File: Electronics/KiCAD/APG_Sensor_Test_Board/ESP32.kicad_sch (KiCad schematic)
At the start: 4 parts, among them U1 ESP32-S3-WROOM-1

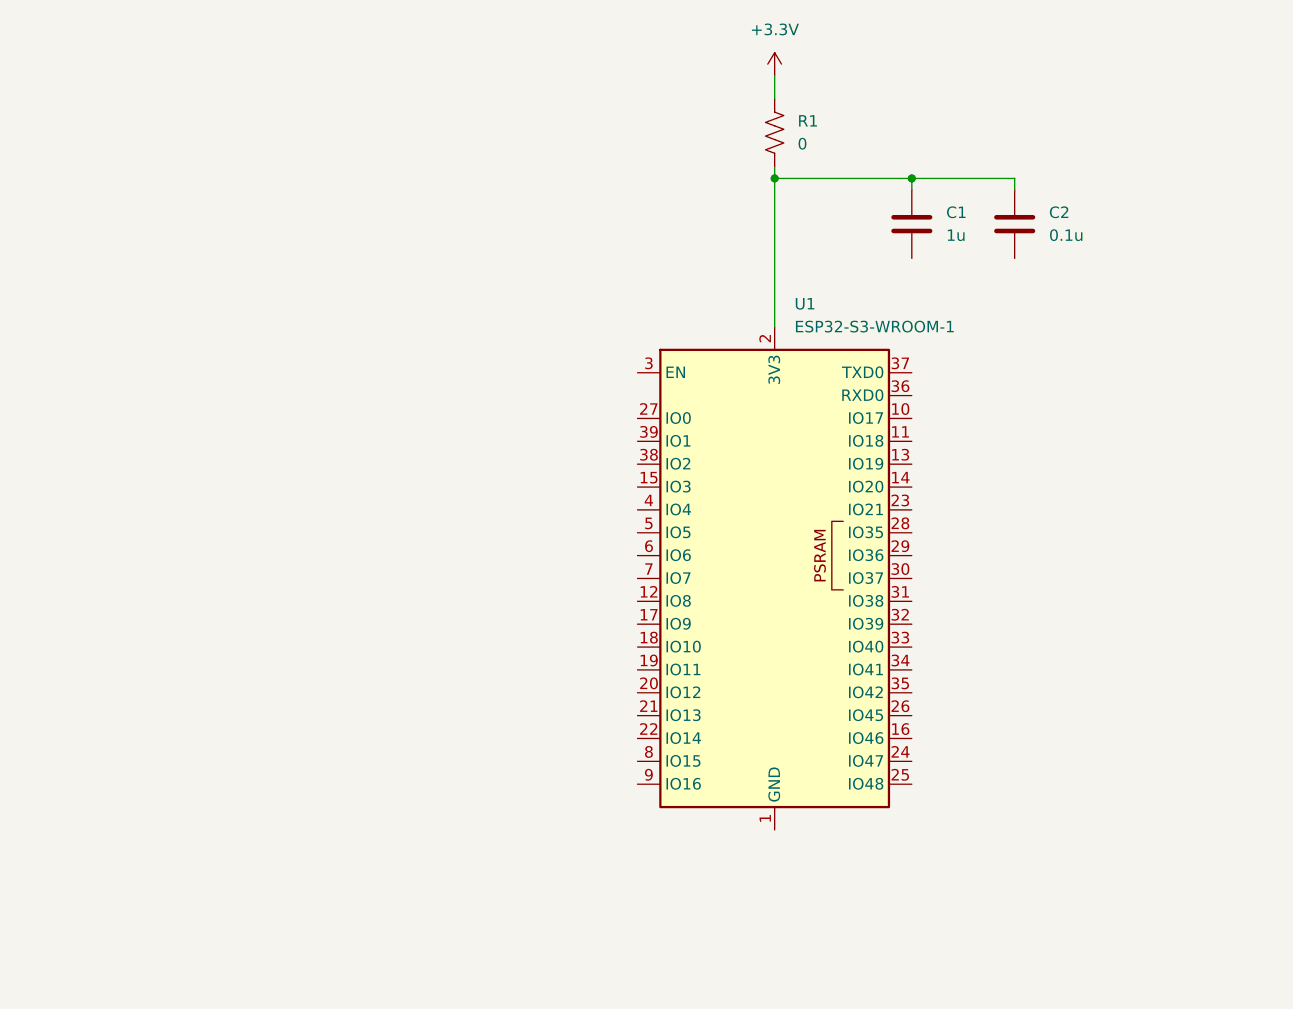
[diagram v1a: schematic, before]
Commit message: Gannon inspection decision to change IMU
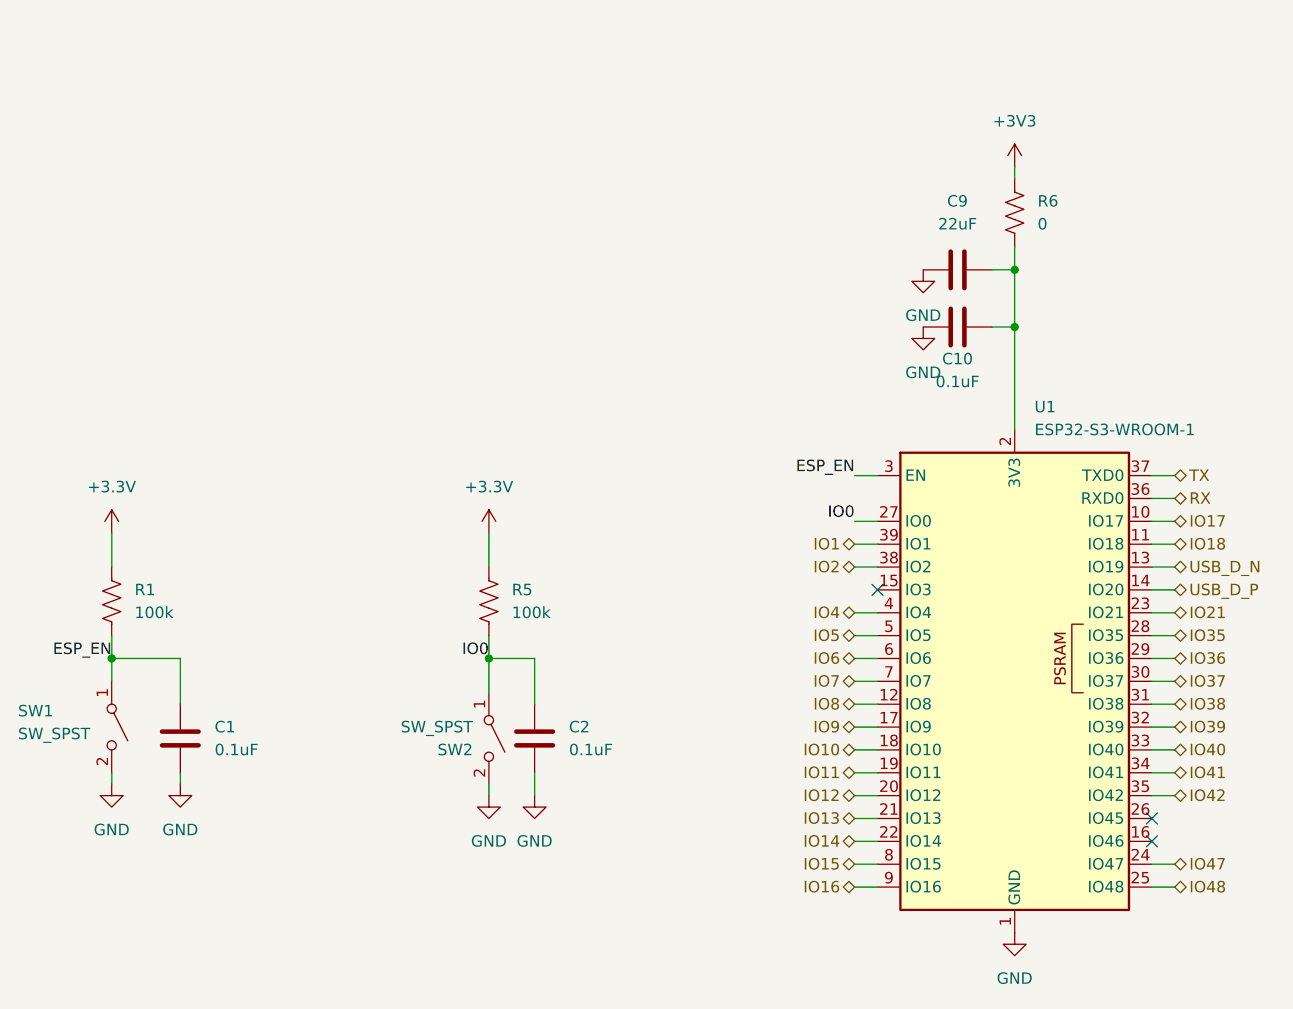
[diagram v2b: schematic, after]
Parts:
- added C10: 0.1uF, symbol Device:C
- added C9: 22uF, symbol Device:C
- added R5: 100k, symbol Device:R_US
- added R6: 0, symbol Device:R_US
- added SW1, SW2: SW_SPST, Button_Switch_SMD:SW_MEC_5GSH9, symbol Switch:SW_SPST
- C1: value 1u -> 0.1uF
- C2: value 0.1u -> 0.1uF
- R1: value 0 -> 100k
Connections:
- net +3.3V: now also R5.1
- net ESP_EN: now reaches C1.1, R1.2
- net ESP_EN: now also U1.3 (EN), SW1.1 (A); no longer C2.1, U1.2 (3V3)
- net GND: now reaches C1.2
- net GND: now also C2.2, U1.1 (GND), U1.40 (GND), U1.41 (GND), C10.1, C9.1, SW1.2 (B), SW2.2 (B)
- net IO17: now reaches U1.10 (IO17)
- net IO18: now reaches U1.11 (IO18)
- net IO8: now reaches U1.12 (IO8)
- net USB_D_N: now reaches U1.13 (IO19)
- net USB_D_P: now reaches U1.14 (IO20)
- net IO9: now reaches U1.17 (IO9)
- net IO10: now reaches U1.18 (IO10)
- net IO11: now reaches U1.19 (IO11)
- net IO12: now reaches U1.20 (IO12)
- net IO13: now reaches U1.21 (IO13)
- net IO14: now reaches U1.22 (IO14)
- net IO21: now reaches U1.23 (IO21)
- net IO47: now reaches U1.24 (IO47)
- net IO48: now reaches U1.25 (IO48)
- net IO0: now reaches U1.27 (IO0)
- net IO0: now also C2.1, R5.2, SW2.1 (A)
- net IO35: now reaches U1.28 (IO35)
- net IO36: now reaches U1.29 (IO36)
- net IO37: now reaches U1.30 (IO37)
- net IO38: now reaches U1.31 (IO38)
- net IO39: now reaches U1.32 (IO39)
- net IO40: now reaches U1.33 (IO40)
- net IO41: now reaches U1.34 (IO41)
- net IO42: now reaches U1.35 (IO42)
- net RX: now reaches U1.36 (RXD0)
- net TX: now reaches U1.37 (TXD0)
- net IO2: now reaches U1.38 (IO2)
- net IO1: now reaches U1.39 (IO1)
- net IO4: now reaches U1.4 (IO4)
- net IO5: now reaches U1.5 (IO5)
- net IO6: now reaches U1.6 (IO6)
- net IO7: now reaches U1.7 (IO7)
- net IO15: now reaches U1.8 (IO15)
- net IO16: now reaches U1.9 (IO16)
- new net: C10.2, C9.2, R6.2, U1.2 (3V3)
- new net +3V3: R6.1
- no-connect marks 0 -> 3

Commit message: reaninotate and begin footprints
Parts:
- C1, C2: footprint (none) -> Capacitor_SMD:C_0805_2012Metric
- C3: renamed from C9; footprint (none) -> Capacitor_SMD:C_0805_2012Metric
- C4: renamed from C10; footprint (none) -> Capacitor_SMD:C_0805_2012Metric
- R3: renamed from R1; footprint (none) -> Resistor_SMD:R_0805_2012Metric
- R4: renamed from R5; footprint (none) -> Resistor_SMD:R_0805_2012Metric
- R5: renamed from R6; footprint (none) -> Resistor_SMD:R_0805_2012Metric
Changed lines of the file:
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@@
 		(dnp no)
 		(fields_autoplaced yes)
-		(property "Reference" "#PWR01"
+		(property "Reference" "#PWR05"
 			(at 68.58 91.44 0)
 			(effects
@@
 			(project "APG_Sensor_Test_Board"
 				(path "/3161be0c-372f-463d-be0a-bab00f344057/597921f3-a65f-46ab-993f-3f9f1b9176d6"
-					(reference "#PWR01")
+					(reference "#PWR05")
 					(unit 1)
 				)
@@
 		(dnp no)
 		(fields_autoplaced yes)
-		(property "Reference" "#PWR025"
+		(property "Reference" "#PWR012"
 			(at 158.75 71.12 0)
 			(effects
@@
 			(project "APG_Sensor_Test_Board"
 				(path "/3161be0c-372f-463d-be0a-bab00f344057/597921f3-a65f-46ab-993f-3f9f1b9176d6"
-					(reference "#PWR025")
+					(reference "#PWR012")
 					(unit 1)
 				)
@@
 		(dnp no)
 		(fields_autoplaced yes)
-		(property "Reference" "#PWR027"
+		(property "Reference" "#PWR014"
 			(at 168.91 138.43 0)
 			(effects
@@
 			(project "APG_Sensor_Test_Board"
 				(path "/3161be0c-372f-463d-be0a-bab00f344057/597921f3-a65f-46ab-993f-3f9f1b9176d6"
-					(reference "#PWR027")
+					(reference "#PWR014")
 					(unit 1)
 				)
@@
 		(on_board yes)
 		(dnp no)
-		(property "Reference" "R1"
+		(property "Reference" "R3"
 			(at 71.12 93.9799 0)
 			(effects
@@
 			)
 		)
-		(property "Footprint" ""
+		(property "Footprint" "Resistor_SMD:R_0805_2012Metric"
 			(at 69.596 95.504 90)
 			(effects
@@
 			(project "APG_Sensor_Test_Board"
 				(path "/3161be0c-372f-463d-be0a-bab00f344057/597921f3-a65f-46ab-993f-3f9f1b9176d6"
-					(reference "R1")
+					(reference "R3")
 					(unit 1)
 				)
@@
 		(dnp no)
 		(fields_autoplaced yes)
-		(property "Reference" "#PWR022"
+		(property "Reference" "#PWR09"
 			(at 110.49 123.19 0)
 			(effects
@@
 			(project "APG_Sensor_Test_Board"
 				(path "/3161be0c-372f-463d-be0a-bab00f344057/597921f3-a65f-46ab-993f-3f9f1b9176d6"
-					(reference "#PWR022")
+					(reference "#PWR09")
 					(unit 1)
 				)
@@
 		(dnp no)
 		(fields_autoplaced yes)
-		(property "Reference" "R6"
+		(property "Reference" "R5"
 			(at 171.45 50.7999 0)
 			(effects
@@
 			)
 		)
-		(property "Footprint" ""
+		(property "Footprint" "Resistor_SMD:R_0805_2012Metric"
 			(at 169.926 52.324 90)
 			(effects
@@
 			(project "APG_Sensor_Test_Board"
 				(path "/3161be0c-372f-463d-be0a-bab00f344057/597921f3-a65f-46ab-993f-3f9f1b9176d6"
-					(reference "R6")
+					(reference "R5")
 					(unit 1)
 				)
@@
 			)
 		)
-		(property "Footprint" ""
+		(property "Footprint" "Capacitor_SMD:C_0805_2012Metric"
 			(at 116.5352 114.3 0)
 			(effects
@@
 		(on_board yes)
 		(dnp no)
-		(property "Reference" "#PWR023"
+		(property "Reference" "#PWR010"
 			(at 115.57 123.19 0)
 			(effects
@@
 			(project "APG_Sensor_Test_Board"
 				(path "/3161be0c-372f-463d-be0a-bab00f344057/597921f3-a65f-46ab-993f-3f9f1b9176d6"
-					(reference "#PWR023")
+					(reference "#PWR010")
 					(unit 1)
 				)
@@
 		(dnp no)
 		(fields_autoplaced yes)
-		(property "Reference" "C9"
+		(property "Reference" "C3"
 			(at 162.56 50.8 90)
 			(effects
@@
 			)
 		)
-		(property "Footprint" ""
+		(property "Footprint" "Capacitor_SMD:C_0805_2012Metric"
 			(at 166.37 57.4548 0)
 			(effects
@@
 			(project "APG_Sensor_Test_Board"
 				(path "/3161be0c-372f-463d-be0a-bab00f344057/597921f3-a65f-46ab-993f-3f9f1b9176d6"
-					(reference "C9")
+					(reference "C3")
 					(unit 1)
 				)
@@
 		(dnp no)
 		(fields_autoplaced yes)
-		(property "Reference" "#PWR026"
+		(property "Reference" "#PWR013"
 			(at 168.91 50.8 0)
 			(effects
@@
 			(project ""
 				(path "/3161be0c-372f-463d-be0a-bab00f344057/597921f3-a65f-46ab-993f-3f9f1b9176d6"
-					(reference "#PWR026")
+					(reference "#PWR013")
 					(unit 1)
 				)
@@
 		(dnp no)
 		(fields_autoplaced yes)
-		(property "Reference" "#PWR020"
+		(property "Reference" "#PWR07"
 			(at 76.2 121.92 0)
 			(effects
@@
 			(project "APG_Sensor_Test_Board"
 				(path "/3161be0c-372f-463d-be0a-bab00f344057/597921f3-a65f-46ab-993f-3f9f1b9176d6"
-					(reference "#PWR020")
+					(reference "#PWR07")
 					(unit 1)
 				)
@@
 		(dnp no)
 		(fields_autoplaced yes)
-		(property "Reference" "R5"
+		(property "Reference" "R4"
 			(at 113.03 93.9799 0)
 			(effects
@@
 			)
 		)
-		(property "Footprint" ""
+		(property "Footprint" "Resistor_SMD:R_0805_2012Metric"
 			(at 111.506 95.504 90)
 			(effects
@@
 			(project "APG_Sensor_Test_Board"
 				(path "/3161be0c-372f-463d-be0a-bab00f344057/597921f3-a65f-46ab-993f-3f9f1b9176d6"
-					(reference "R5")
+					(reference "R4")
 					(unit 1)
 				)
@@
 		(dnp no)
 		(fields_autoplaced yes)
-		(property "Reference" "#PWR019"
+		(property "Reference" "#PWR06"
 			(at 68.58 121.92 0)
 			(effects
@@
 			(project "APG_Sensor_Test_Board"
 				(path "/3161be0c-372f-463d-be0a-bab00f344057/597921f3-a65f-46ab-993f-3f9f1b9176d6"
-					(reference "#PWR019")
+					(reference "#PWR06")
 					(unit 1)
 				)
@@
 		(dnp no)
 		(fields_autoplaced yes)
-		(property "Reference" "#PWR024"
+		(property "Reference" "#PWR011"
 			(at 158.75 64.77 0)
 			(effects
@@
 			(project "APG_Sensor_Test_Board"
 				(path "/3161be0c-372f-463d-be0a-bab00f344057/597921f3-a65f-46ab-993f-3f9f1b9176d6"
-					(reference "#PWR024")
+					(reference "#PWR011")
 					(unit 1)
 				)
@@
 		(on_board yes)
 		(dnp no)
-		(property "Reference" "C10"
+		(property "Reference" "C4"
 			(at 162.56 68.326 90)
 			(effects
@@
 			)
 		)
-		(property "Footprint" ""
+		(property "Footprint" "Capacitor_SMD:C_0805_2012Metric"
 			(at 166.37 63.8048 0)
 			(effects
@@
 			(project "APG_Sensor_Test_Board"
 				(path "/3161be0c-372f-463d-be0a-bab00f344057/597921f3-a65f-46ab-993f-3f9f1b9176d6"
-					(reference "C10")
+					(reference "C4")
 					(unit 1)
 				)
@@
 			)
 		)
-		(property "Footprint" ""
+		(property "Footprint" "Capacitor_SMD:C_0805_2012Metric"
 			(at 77.1652 114.3 0)
 			(effects
@@
 		(dnp no)
 		(fields_autoplaced yes)
-		(property "Reference" "#PWR021"
+		(property "Reference" "#PWR08"
 			(at 110.49 91.44 0)
 			(effects
@@
 			(project "APG_Sensor_Test_Board"
 				(path "/3161be0c-372f-463d-be0a-bab00f344057/597921f3-a65f-46ab-993f-3f9f1b9176d6"
-					(reference "#PWR021")
-					(unit 1)
-				)
+					(reference "#PWR08")
+					(unit 1)
+				)

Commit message: MOved IMU and HIGH G to SPI other misc changes
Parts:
- removed R3, R4: 100k, Resistor_SMD:R_0805_2012Metric, symbol Device:R_US
- removed R5: 0, Resistor_SMD:R_0805_2012Metric, symbol Device:R_US
- added R10, R9: 100k, Resistor_SMD:R_0805_2012Metric, symbol Device:R
- added R11: 0, Resistor_SMD:R_0805_2012Metric, symbol Device:R
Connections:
- net +3.3V: now also R10.1, R9.1
- net +3V3: now also R11.1
- net ESP_EN: now also R9.2
- net IO0: now also R10.2
- net IO3: now reaches U1.15 (IO3)
- net at C3.2, C4.2, U1.2 (3V3): now also R11.2
- no-connect marks 3 -> 2
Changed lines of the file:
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@@
 		(at 184.15 121.92)
 	)
-	(no_connect
-		(at 153.67 93.98)
-	)
 	(wire
 		(pts
@@
 		(pts
 			(xy 151.13 96.52) (xy 153.67 96.52)
+		)
+		(stroke
+			(width 0)
+			(type default)
+		)
+	)
+	(wire
+		(pts
+			(xy 151.13 93.98) (xy 153.67 93.98)
 		)
 		(stroke
@@
 		(shape bidirectional)
 		(at 151.13 99.06 180)
+		(fields_autoplaced yes)
+		(effects
+			(font
+				(size 1.27 1.27)
+			)
+			(justify right)
+		)
+	)
+	(hierarchical_label "IO3"
+		(shape bidirectional)
+		(at 151.13 93.98 180)
 		(fields_autoplaced yes)
 		(effects
@@
 	)
 	(symbol
+		(lib_id "Device:R")
+		(at 68.58 95.25 0)
+		(unit 1)
+		(exclude_from_sim no)
+		(in_bom yes)
+		(on_board yes)
+		(dnp no)
+		(fields_autoplaced yes)
+		(property "Reference" "R9"
+			(at 71.12 93.9799 0)
+			(effects
+				(font
+					(size 1.27 1.27)
+				)
+				(justify left)
+			)
+		)
+		(property "Value" "100k"
+			(at 71.12 96.5199 0)
+			(effects
+				(font
+					(size 1.27 1.27)
+				)
+				(justify left)
+			)
+		)
+		(property "Footprint" "Resistor_SMD:R_0805_2012Metric"
+			(at 66.802 95.25 90)
+			(effects
+				(font
+					(size 1.27 1.27)
+				)
+				(hide yes)
+			)
+		)
+		(property "Datasheet" "~"
+			(at 68.58 95.25 0)
+			(effects
+				(font
+					(size 1.27 1.27)
+				)
+				(hide yes)
+			)
+		)
+		(property "Description" "Resistor"
+			(at 68.58 95.25 0)
+			(effects
+				(font
+					(size 1.27 1.27)
+				)
+				(hide yes)
+			)
+		)
+		(pin "1"
+		)
+		(pin "2"
+		)
+		(instances
+			(project "APG_Sensor_Test_Board"
+				(path "/3161be0c-372f-463d-be0a-bab00f344057/597921f3-a65f-46ab-993f-3f9f1b9176d6"
+					(reference "R9")
+					(unit 1)
+				)
+			)
+		)
+	)
+	(symbol
 		(lib_id "RF_Module:ESP32-S3-WROOM-1")
 		(at 168.91 104.14 0)
@@
 	)
 	(symbol
-		(lib_id "Device:R_US")
-		(at 68.58 95.25 0)
-		(unit 1)
-		(exclude_from_sim no)
-		(in_bom yes)
-		(on_board yes)
-		(dnp no)
-		(property "Reference" "R3"
-			(at 71.12 93.9799 0)
-			(effects
-				(font
-					(size 1.27 1.27)
-				)
-				(justify left)
-			)
-		)
-		(property "Value" "100k"
-			(at 71.12 96.5199 0)
-			(effects
-				(font
-					(size 1.27 1.27)
-				)
-				(justify left)
-			)
-		)
-		(property "Footprint" "Resistor_SMD:R_0805_2012Metric"
-			(at 69.596 95.504 90)
-			(effects
-				(font
-					(size 1.27 1.27)
-				)
-				(hide yes)
-			)
-		)
-		(property "Datasheet" "~"
-			(at 68.58 95.25 0)
-			(effects
-				(font
-					(size 1.27 1.27)
-				)
-				(hide yes)
-			)
-		)
-		(property "Description" "Resistor, US symbol"
-			(at 68.58 95.25 0)
-			(effects
-				(font
-					(size 1.27 1.27)
-				)
-				(hide yes)
-			)
-		)
-		(pin "1"
-		)
-		(pin "2"
-		)
-		(instances
-			(project "APG_Sensor_Test_Board"
-				(path "/3161be0c-372f-463d-be0a-bab00f344057/597921f3-a65f-46ab-993f-3f9f1b9176d6"
-					(reference "R3")
-					(unit 1)
-				)
-			)
-		)
-	)
-	(symbol
 		(lib_id "power:GND")
 		(at 110.49 116.84 0)
@@
 				(path "/3161be0c-372f-463d-be0a-bab00f344057/597921f3-a65f-46ab-993f-3f9f1b9176d6"
 					(reference "#PWR09")
-					(unit 1)
-				)
-			)
-		)
-	)
-	(symbol
-		(lib_id "Device:R_US")
-		(at 168.91 52.07 0)
-		(unit 1)
-		(exclude_from_sim no)
-		(in_bom yes)
-		(on_board yes)
-		(dnp no)
-		(fields_autoplaced yes)
-		(property "Reference" "R5"
-			(at 171.45 50.7999 0)
-			(effects
-				(font
-					(size 1.27 1.27)
-				)
-				(justify left)
-			)
-		)
-		(property "Value" "0"
-			(at 171.45 53.3399 0)
-			(effects
-				(font
-					(size 1.27 1.27)
-				)
-				(justify left)
-			)
-		)
-		(property "Footprint" "Resistor_SMD:R_0805_2012Metric"
-			(at 169.926 52.324 90)
-			(effects
-				(font
-					(size 1.27 1.27)
-				)
-				(hide yes)
-			)
-		)
-		(property "Datasheet" "~"
-			(at 168.91 52.07 0)
-			(effects
-				(font
-					(size 1.27 1.27)
-				)
-				(hide yes)
-			)
-		)
-		(property "Description" "Resistor, US symbol"
-			(at 168.91 52.07 0)
-			(effects
-				(font
-					(size 1.27 1.27)
-				)
-				(hide yes)
-			)
-		)
-		(pin "1"
-		)
-		(pin "2"
-		)
-		(instances
-			(project "APG_Sensor_Test_Board"
-				(path "/3161be0c-372f-463d-be0a-bab00f344057/597921f3-a65f-46ab-993f-3f9f1b9176d6"
-					(reference "R5")
 					(unit 1)
 				)
@@
 				(path "/3161be0c-372f-463d-be0a-bab00f344057/597921f3-a65f-46ab-993f-3f9f1b9176d6"
 					(reference "C2")
+					(unit 1)
+				)
+			)
+		)
+	)
+	(symbol
+		(lib_id "Device:R")
+		(at 110.49 95.25 0)
+		(unit 1)
+		(exclude_from_sim no)
+		(in_bom yes)
+		(on_board yes)
+		(dnp no)
+		(fields_autoplaced yes)
+		(property "Reference" "R10"
+			(at 113.03 93.9799 0)
+			(effects
+				(font
+					(size 1.27 1.27)
+				)
+				(justify left)
+			)
+		)
+		(property "Value" "100k"
+			(at 113.03 96.5199 0)
+			(effects
+				(font
+					(size 1.27 1.27)
+				)
+				(justify left)
+			)
+		)
+		(property "Footprint" "Resistor_SMD:R_0805_2012Metric"
+			(at 108.712 95.25 90)
+			(effects
+				(font
+					(size 1.27 1.27)
+				)
+				(hide yes)
+			)
+		)
+		(property "Datasheet" "~"
+			(at 110.49 95.25 0)
+			(effects
+				(font
+					(size 1.27 1.27)
+				)
+				(hide yes)
+			)
+		)
+		(property "Description" "Resistor"
+			(at 110.49 95.25 0)
+			(effects
+				(font
+					(size 1.27 1.27)
+				)
+				(hide yes)
+			)
+		)
+		(pin "1"
+		)
+		(pin "2"
+		)
+		(instances
+			(project "APG_Sensor_Test_Board"
+				(path "/3161be0c-372f-463d-be0a-bab00f344057/597921f3-a65f-46ab-993f-3f9f1b9176d6"
+					(reference "R10")
 					(unit 1)
 				)
@@
 	)
 	(symbol
-		(lib_id "Device:R_US")
-		(at 110.49 95.25 0)
-		(unit 1)
-		(exclude_from_sim no)
-		(in_bom yes)
-		(on_board yes)
-		(dnp no)
-		(fields_autoplaced yes)
-		(property "Reference" "R4"
-			(at 113.03 93.9799 0)
-			(effects
-				(font
-					(size 1.27 1.27)
-				)
-				(justify left)
-			)
-		)
-		(property "Value" "100k"
-			(at 113.03 96.5199 0)
-			(effects
-				(font
-					(size 1.27 1.27)
-				)
-				(justify left)
-			)
-		)
-		(property "Footprint" "Resistor_SMD:R_0805_2012Metric"
-			(at 111.506 95.504 90)
-			(effects
-				(font
-					(size 1.27 1.27)
-				)
-				(hide yes)
-			)
-		)
-		(property "Datasheet" "~"
-			(at 110.49 95.25 0)
-			(effects
-				(font
-					(size 1.27 1.27)
-				)
-				(hide yes)
-			)
-		)
-		(property "Description" "Resistor, US symbol"
-			(at 110.49 95.25 0)
-			(effects
-				(font
-					(size 1.27 1.27)
-				)
-				(hide yes)
-			)
-		)
-		(pin "1"
-		)
-		(pin "2"
-		)
-		(instances
-			(project "APG_Sensor_Test_Board"
-				(path "/3161be0c-372f-463d-be0a-bab00f344057/597921f3-a65f-46ab-993f-3f9f1b9176d6"
-					(reference "R4")
-					(unit 1)
-				)
-			)
-		)
-	)
-	(symbol
 		(lib_id "Switch:SW_SPST")
 		(at 110.49 110.49 270)
@@
 					(unit 1)
 				)
+			)
+		)
+	)
+	(symbol
+		(lib_id "Device:R")
+		(at 168.91 52.07 0)
+		(unit 1)
+		(exclude_from_sim no)
+		(in_bom yes)
+		(on_board yes)
+		(dnp no)
+		(fields_autoplaced yes)
+		(property "Reference" "R11"
+			(at 171.45 50.7999 0)
+			(effects
+				(font
+					(size 1.27 1.27)
+				)
+				(justify left)
+			)
+		)
+		(property "Value" "0"
+			(at 171.45 53.3399 0)
+			(effects
+				(font
+					(size 1.27 1.27)
+				)
+				(justify left)
+			)
+		)
+		(property "Footprint" "Resistor_SMD:R_0805_2012Metric"
+			(at 167.132 52.07 90)
+			(effects
+				(font
+					(size 1.27 1.27)
+				)
+				(hide yes)
+			)
+		)
+		(property "Datasheet" "~"
+			(at 168.91 52.07 0)
+			(effects
+				(font
+					(size 1.27 1.27)
+				)
+				(hide yes)
+			)
+		)
+		(property "Description" "Resistor"
+			(at 168.91 52.07 0)
+			(effects
+				(font
+					(size 1.27 1.27)
+				)
+				(hide yes)
+			)
+		)
+		(pin "1"
+		)
+		(pin "2"
+		)
+		(instances
+			(project "APG_Sensor_Test_Board"
+				(path "/3161be0c-372f-463d-be0a-bab00f344057/597921f3-a65f-46ab-993f-3f9f1b9176d6"
+					(reference "R11")
+					(unit 1)
+				)

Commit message: TVS protection began layout
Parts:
- SW1, SW2: footprint Button_Switch_SMD:SW_MEC_5GSH9 -> Button_Switch_THT:SW_PUSH_6mm_H5mm
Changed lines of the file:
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@@
 			)
 		)
-		(property "Footprint" "Button_Switch_SMD:SW_MEC_5GSH9"
+		(property "Footprint" "Button_Switch_THT:SW_PUSH_6mm_H5mm"
 			(at 68.58 109.22 0)
 			(effects
@@
 			)
 		)
-		(property "Footprint" "Button_Switch_SMD:SW_MEC_5GSH9"
+		(property "Footprint" "Button_Switch_THT:SW_PUSH_6mm_H5mm"
 			(at 110.49 110.49 0)
 			(effects
